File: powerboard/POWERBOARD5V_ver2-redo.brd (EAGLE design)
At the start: 83 x 42 mm, 55 parts, among them IC1 TPS5420, IC2 TPS5420

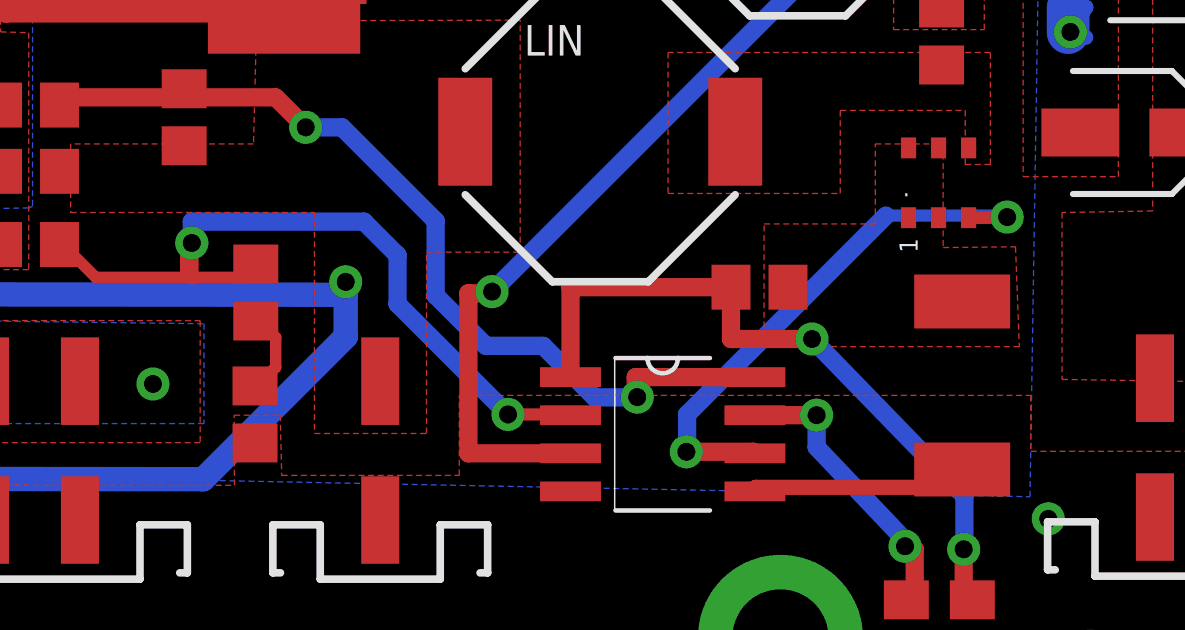
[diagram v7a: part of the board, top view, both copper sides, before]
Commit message: mostly silkscreen fixes
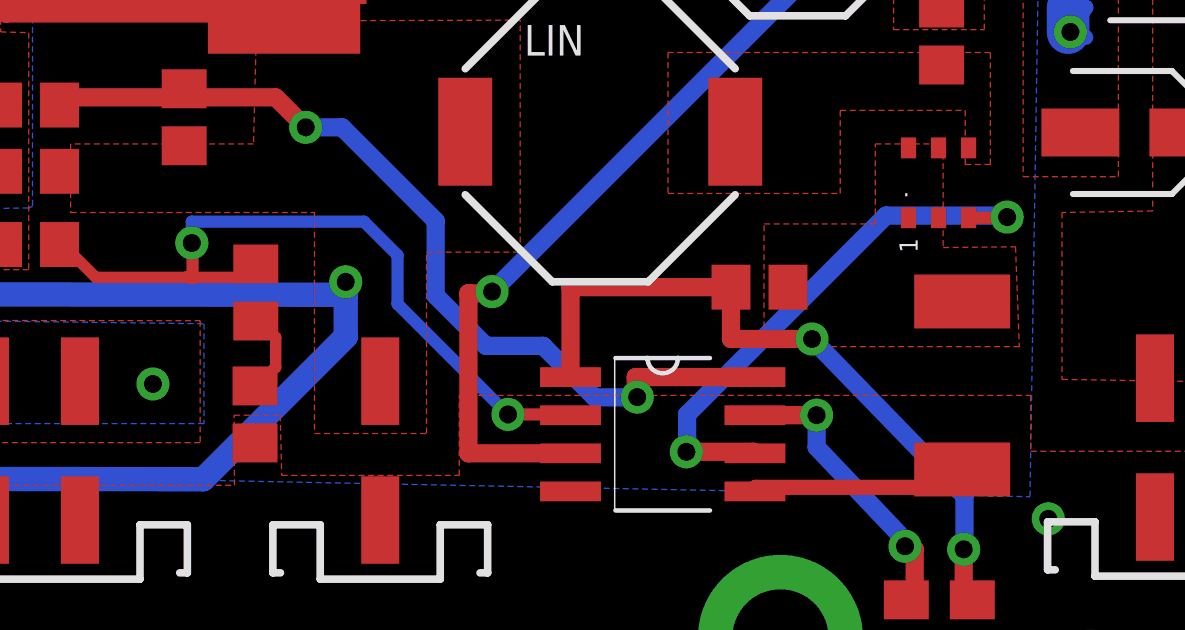
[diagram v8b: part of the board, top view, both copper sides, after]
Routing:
- net N$3: track 26.2 -> 25.2 mm
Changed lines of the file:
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@@
 <wire x1="62.7126" y1="10.16" x2="62.7126" y2="11.43" width="0.6096" layer="16"/>
 <wire x1="62.7126" y1="11.43" x2="69.342" y2="18.0594" width="0.6096" layer="16"/>
-<wire x1="69.342" y1="18.0594" x2="73" y2="18.0594" width="0.4064" layer="16"/>
+<wire x1="69.342" y1="18.0594" x2="73" y2="18.0594" width="0.6096" layer="16"/>
 <wire x1="73" y1="18.0594" x2="73.3298" y2="18.0594" width="0.4064" layer="16"/>
 <wire x1="73.3298" y1="18.0594" x2="73.3806" y2="18.0086" width="0.4064" layer="16"/>
@@
 <wire x1="56.7436" y1="11.43" x2="58.4454" y2="11.43" width="0.4064" layer="1"/>
 <wire x1="58.4454" y1="11.43" x2="58.4708" y2="11.4554" width="0.4064" layer="1"/>
-<wire x1="56.7436" y1="11.43" x2="53.0606" y2="15.113" width="0.6096" layer="16"/>
-<wire x1="53.0606" y1="15.113" x2="53.0606" y2="16.7386" width="0.6096" layer="16"/>
-<wire x1="53.0606" y1="16.7386" x2="51.943" y2="17.8562" width="0.6096" layer="16"/>
-<wire x1="51.943" y1="17.8562" x2="46.2026" y2="17.8562" width="0.6096" layer="16"/>
-<wire x1="46.2026" y1="17.8562" x2="46.2026" y2="17.145" width="0.6096" layer="16"/>
+<wire x1="56.7436" y1="11.43" x2="53.0606" y2="15.113" width="0.4064" layer="16"/>
+<wire x1="53.0606" y1="15.113" x2="53.0606" y2="16.7386" width="0.4064" layer="16"/>
+<wire x1="53.0606" y1="16.7386" x2="51.943" y2="17.8562" width="0.4064" layer="16"/>
+<wire x1="51.943" y1="17.8562" x2="46.2026" y2="17.8562" width="0.4064" layer="16"/>
+<wire x1="46.2026" y1="17.8562" x2="46.2026" y2="17.145" width="0.4064" layer="16"/>
 <wire x1="46" y1="16" x2="46.2026" y2="15.9766" width="0.381" layer="1"/>
-<wire x1="46" y1="17" x2="46" y2="16" width="0.381" layer="1"/>
-<wire x1="46" y1="17" x2="46.2026" y2="17.145" width="0.381" layer="1"/>
 <wire x1="58.4454" y1="11.43" x2="58.8264" y2="11.4046" width="0" layer="19" extent="1-1"/>
+<wire x1="46.228" y1="16.8656" x2="46.2026" y2="16.8656" width="0.4064" layer="1"/>
+<wire x1="46.2026" y1="16.8656" x2="46.2026" y2="17.145" width="0.4064" layer="1"/>
 </signal>
 </signals>
